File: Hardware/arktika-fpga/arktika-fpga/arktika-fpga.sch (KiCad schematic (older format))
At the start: 4 parts

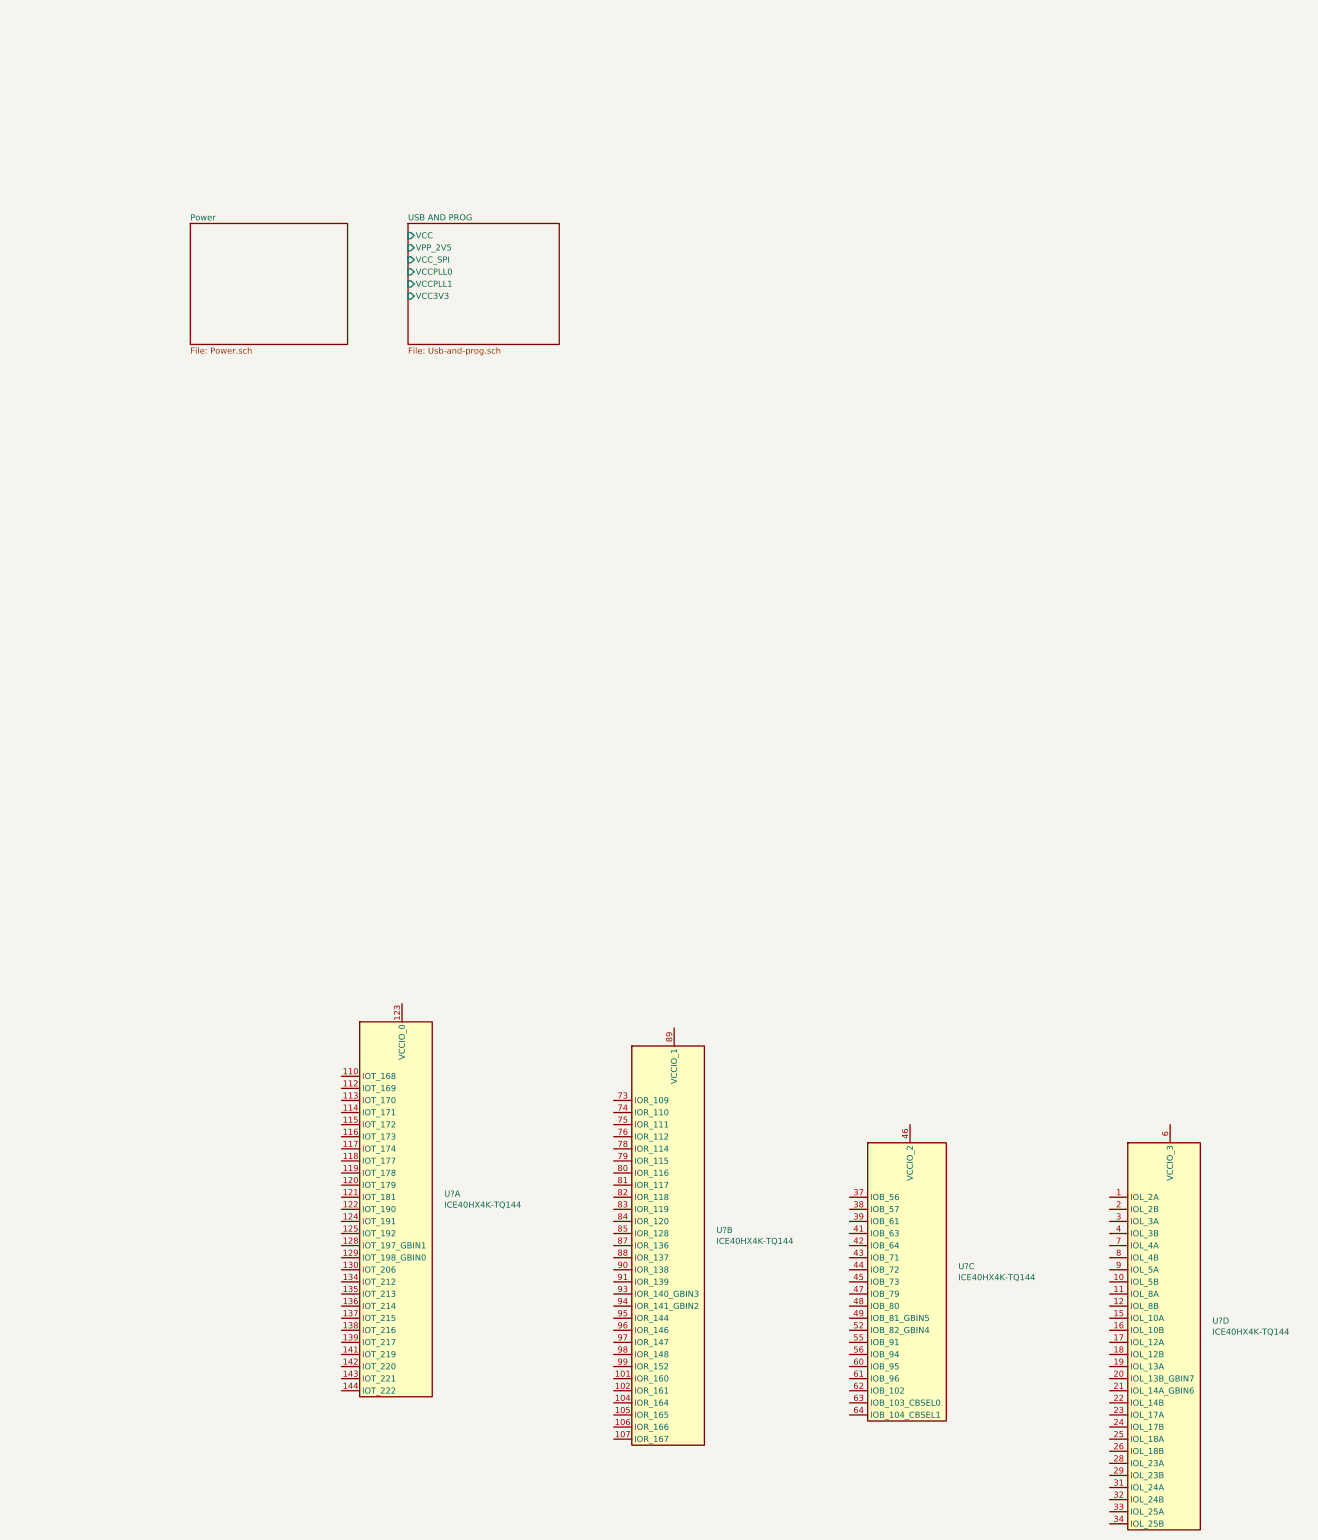
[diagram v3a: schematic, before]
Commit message: Added designators, some io, and some peripherals
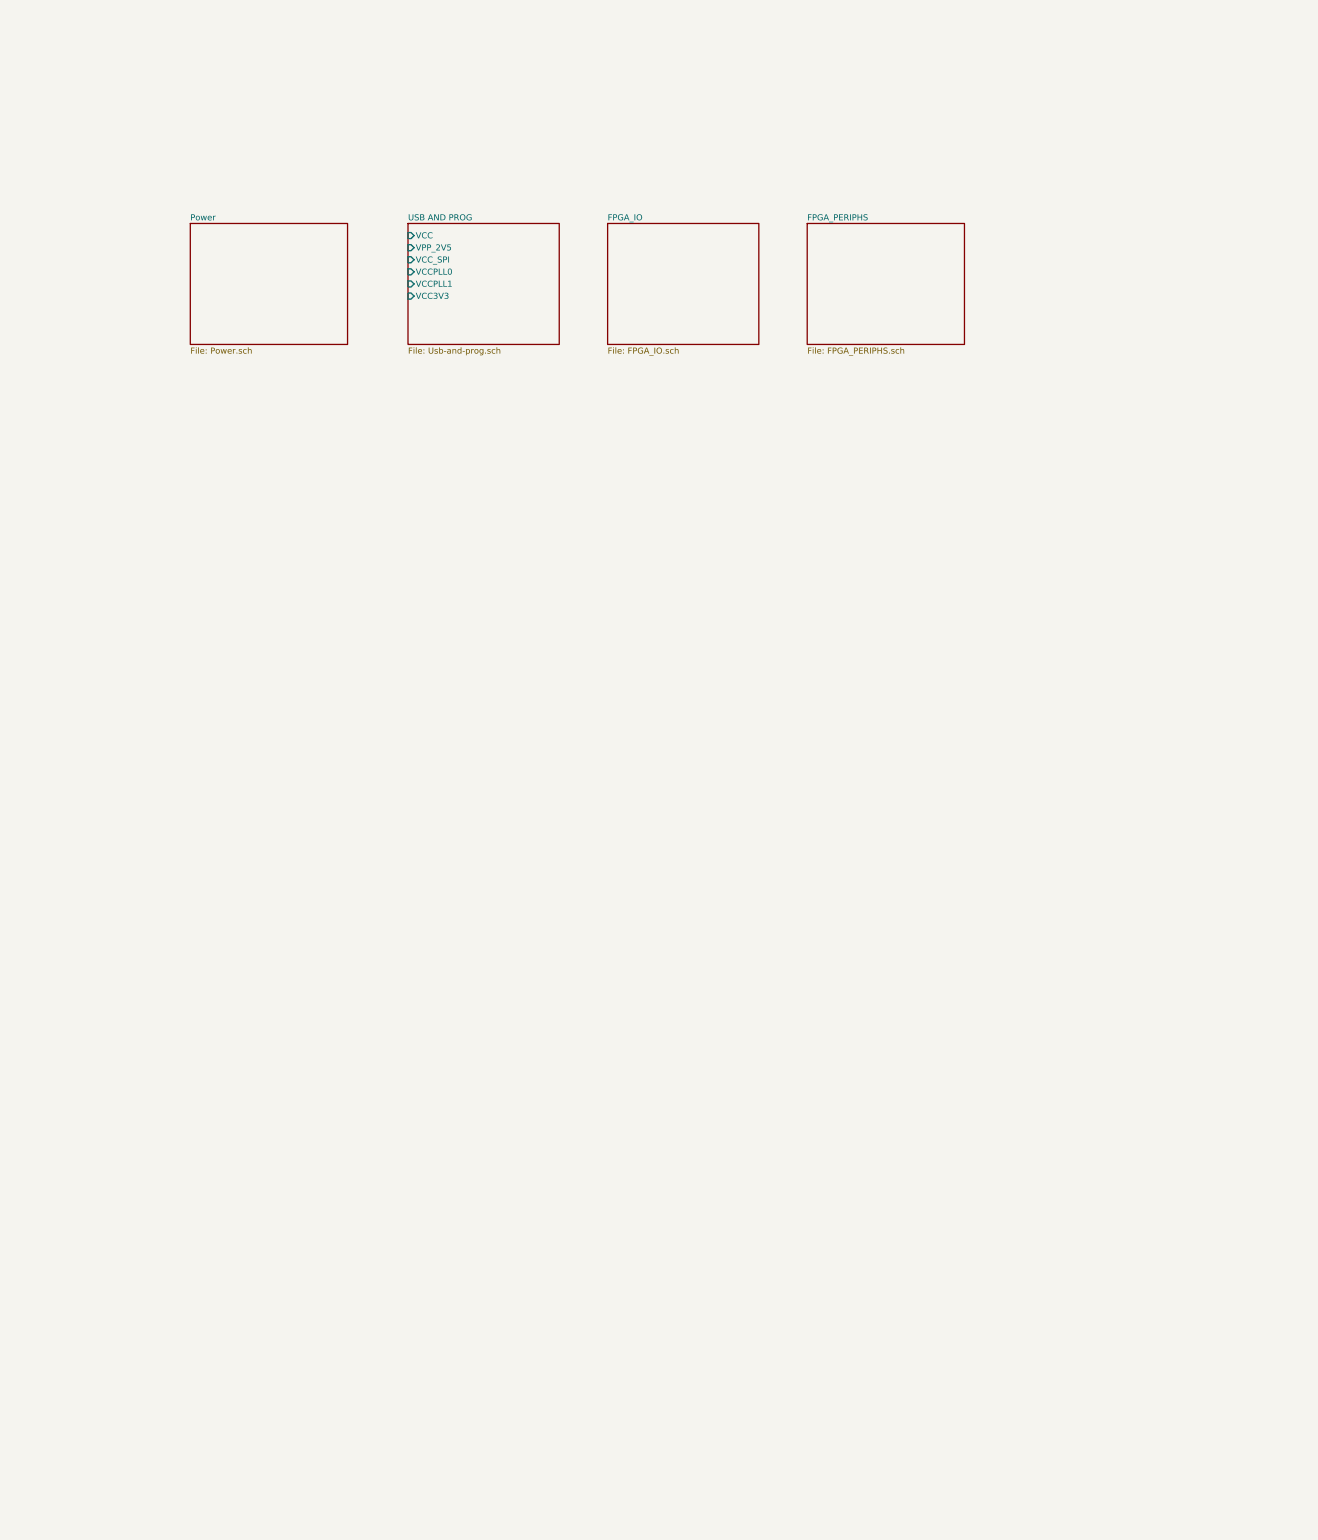
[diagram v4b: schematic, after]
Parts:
- removed U? (x4): ICE40HX4K-TQ144, Package_QFP:TQFP-144_20x20mm_P0.5mm, symbol FPGA_Lattice:ICE40HX4K-TQ144
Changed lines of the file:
@@
 $Descr A4 11693 8268
 encoding utf-8
-Sheet 1 3
+Sheet 1 5
 Title "Arktika FPGA"
-Date "2020-07-26"
+Date "2020-07-28"
 Rev ""
 Comp "Author: Afonso Muralha"
@@
 Comment4 ""
 $EndDescr
-$Comp
-L FPGA_Lattice:ICE40HX4K-TQ144 U?
-U 1 1 5F1D1844
-P 4300 11350
-F 0 "U?" H 4649 11578 50  0000 L CNN
-F 1 "ICE40HX4K-TQ144" H 4649 11487 50  0000 L CNN
-F 2 "Package_QFP:TQFP-144_20x20mm_P0.5mm" H 5300 9450 50  0001 R CNN
-F 3 "http://www.latticesemi.com/Products/FPGAandCPLD/iCE40" H 3300 13850 50  0001 C CNN
-	1    4300 11350
-	1    0    0    -1
-$EndComp
-$Comp
-L FPGA_Lattice:ICE40HX4K-TQ144 U?
-U 2 1 5F1D412B
-P 6550 11650
-F 0 "U?" H 6899 11878 50  0000 L CNN
-F 1 "ICE40HX4K-TQ144" H 6899 11787 50  0000 L CNN
-F 2 "Package_QFP:TQFP-144_20x20mm_P0.5mm" H 7550 9750 50  0001 R CNN
-F 3 "http://www.latticesemi.com/Products/FPGAandCPLD/iCE40" H 5550 14150 50  0001 C CNN
-	2    6550 11650
-	1    0    0    -1
-$EndComp
-$Comp
-L FPGA_Lattice:ICE40HX4K-TQ144 U?
-U 3 1 5F1D7E9E
-P 8500 11950
-F 0 "U?" H 8899 12178 50  0000 L CNN
-F 1 "ICE40HX4K-TQ144" H 8899 12087 50  0000 L CNN
-F 2 "Package_QFP:TQFP-144_20x20mm_P0.5mm" H 9500 10050 50  0001 R CNN
-F 3 "http://www.latticesemi.com/Products/FPGAandCPLD/iCE40" H 7500 14450 50  0001 C CNN
-	3    8500 11950
-	1    0    0    -1
-$EndComp
-$Comp
-L FPGA_Lattice:ICE40HX4K-TQ144 U?
-U 4 1 5F1DC6C8
-P 10650 12350
-F 0 "U?" H 10999 12528 50  0000 L CNN
-F 1 "ICE40HX4K-TQ144" H 10999 12437 50  0000 L CNN
-F 2 "Package_QFP:TQFP-144_20x20mm_P0.5mm" H 11650 10450 50  0001 R CNN
-F 3 "http://www.latticesemi.com/Products/FPGAandCPLD/iCE40" H 9650 14850 50  0001 C CNN
-	4    10650 12350
-	1    0    0    -1
-$EndComp
 $Sheet
 S 2550 3100 1300 1000
@@
 F7 "VCC3V3" I L 4350 3700 50
 $EndSheet
+$Sheet
+S 6000 3100 1250 1000
+U 5F516611
+F0 "FPGA_IO" 50
+F1 "FPGA_IO.sch" 50
+$EndSheet
+$Sheet
+S 7650 3100 1300 1000
+U 5F72015E
+F0 "FPGA_PERIPHS" 50
+F1 "FPGA_PERIPHS.sch" 50
+$EndSheet
 $EndSCHEMATC

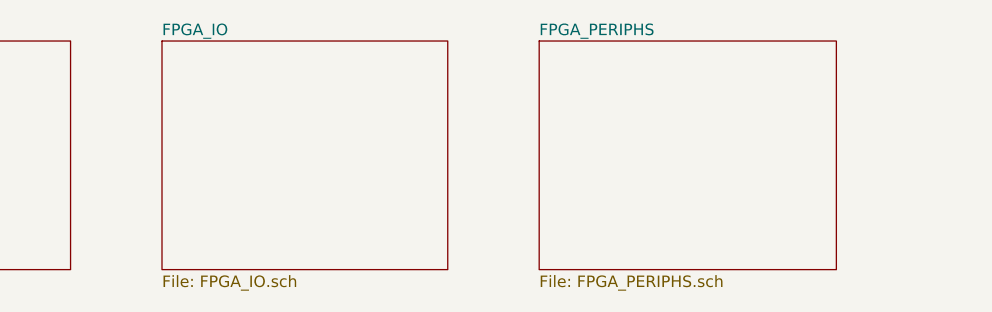
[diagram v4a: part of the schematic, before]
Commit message: Minor fixes, added peripheral buses, added annotations and added crystal datasheets
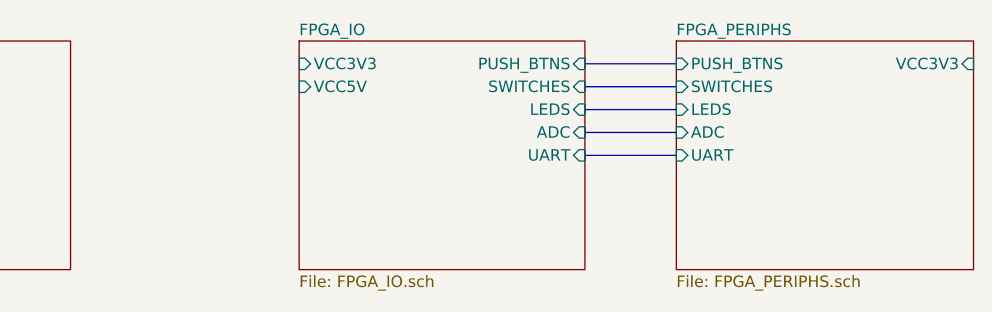
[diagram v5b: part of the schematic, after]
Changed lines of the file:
@@
 Sheet 1 5
 Title "Arktika FPGA"
-Date "2020-07-28"
+Date "2020-07-29"
 Rev ""
 Comp "Author: Afonso Muralha"
@@
 $EndSheet
 $Sheet
-S 6000 3100 1250 1000
+S 6600 3100 1250 1000
 U 5F516611
 F0 "FPGA_IO" 50
 F1 "FPGA_IO.sch" 50
+F2 "VCC3V3" I L 6600 3200 50
+F3 "VCC5V" I L 6600 3300 50
+F4 "PUSH_BTNS" I R 7850 3200 50
+F5 "SWITCHES" I R 7850 3300 50
+F6 "LEDS" I R 7850 3400 50
+F7 "ADC" I R 7850 3500 50
+F8 "UART" I R 7850 3600 50
 $EndSheet
 $Sheet
-S 7650 3100 1300 1000
+S 8250 3100 1300 1000
 U 5F72015E
 F0 "FPGA_PERIPHS" 50
 F1 "FPGA_PERIPHS.sch" 50
+F2 "PUSH_BTNS" I L 8250 3200 50
+F3 "SWITCHES" I L 8250 3300 50
+F4 "LEDS" I L 8250 3400 50
+F5 "ADC" I L 8250 3500 50
+F6 "UART" I L 8250 3600 50
+F7 "VCC3V3" I R 9550 3200 50
 $EndSheet
+Wire Bus Line
+	7850 3200 8250 3200
+Wire Bus Line
+	7850 3300 8250 3300
+Wire Bus Line
+	7850 3400 8250 3400
+Wire Bus Line
+	7850 3500 8250 3500
+Wire Bus Line
+	7850 3600 8250 3600
 $EndSCHEMATC

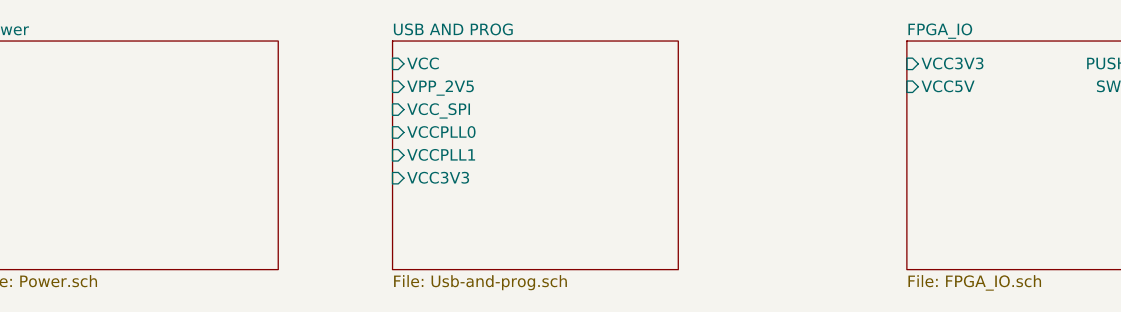
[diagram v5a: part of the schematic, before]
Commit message: Added alternate power intput. Update some designators. Added fpga crystal
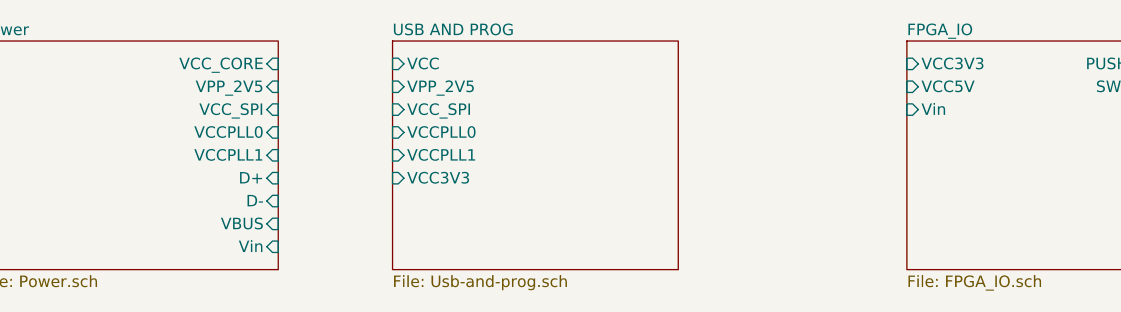
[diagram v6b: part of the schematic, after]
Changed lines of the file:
@@
 F0 "Power" 50
 F1 "Power.sch" 50
+F2 "VCC_CORE" I R 3850 3200 50
+F3 "VPP_2V5" I R 3850 3300 50
+F4 "VCC_SPI" I R 3850 3400 50
+F5 "VCCPLL0" I R 3850 3500 50
+F6 "VCCPLL1" I R 3850 3600 50
+F7 "D+" I R 3850 3700 50
+F8 "D-" I R 3850 3800 50
+F9 "VBUS" I R 3850 3900 50
+F10 "Vin" I R 3850 4000 50
 $EndSheet
 $Sheet
@@
 F7 "ADC" I R 7850 3500 50
 F8 "UART" I R 7850 3600 50
+F9 "Vin" I L 6600 3400 50
 $EndSheet
 $Sheet

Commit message: Misc changes and fixes
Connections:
- net labels added: GND, VCC3V3, VCC5V, VIN
- wire segments 0 -> 19
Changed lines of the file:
@@
 $EndDescr
 $Sheet
-S 2550 3100 1300 1000
+S 2550 3100 1300 1050
 U 5F3E98C5
 F0 "Power" 50
@@
 F7 "D+" I R 3850 3700 50
 F8 "D-" I R 3850 3800 50
-F9 "VBUS" I R 3850 3900 50
-F10 "Vin" I R 3850 4000 50
+F9 "Vin" I R 3850 4100 50
+F10 "VCC3V3" I R 3850 4000 50
+F11 "VCC5V" I R 3850 3900 50
+F12 "GND" I L 2550 4050 50
 $EndSheet
 $Sheet
@@
 F0 "USB AND PROG" 50
 F1 "Usb-and-prog.sch" 50
-F2 "VCC" I L 4350 3200 50
-F3 "VPP_2V5" I L 4350 3300 50
-F4 "VCC_SPI" I L 4350 3400 50
-F5 "VCCPLL0" I L 4350 3500 50
-F6 "VCCPLL1" I L 4350 3600 50
-F7 "VCC3V3" I L 4350 3700 50
+F2 "VPP_2V5" I L 4350 3300 50
+F3 "VCC_SPI" I L 4350 3400 50
+F4 "VCCPLL0" I L 4350 3500 50
+F5 "VCCPLL1" I L 4350 3600 50
+F6 "VCC3V3" I L 4350 4000 50
+F7 "VCC_CORE" I L 4350 3200 50
+F8 "D+" I L 4350 3700 50
+F9 "D-" I L 4350 3800 50
+F10 "VBUS" I L 4350 3900 50
+F11 "GND" I R 5600 4050 50
 $EndSheet
 $Sheet
-S 6600 3100 1250 1000
+S 6300 3100 1250 1000
 U 5F516611
 F0 "FPGA_IO" 50
 F1 "FPGA_IO.sch" 50
-F2 "VCC3V3" I L 6600 3200 50
-F3 "VCC5V" I L 6600 3300 50
-F4 "PUSH_BTNS" I R 7850 3200 50
-F5 "SWITCHES" I R 7850 3300 50
-F6 "LEDS" I R 7850 3400 50
-F7 "ADC" I R 7850 3500 50
-F8 "UART" I R 7850 3600 50
-F9 "Vin" I L 6600 3400 50
+F2 "VCC3V3" I L 6300 3200 50
+F3 "VCC5V" I L 6300 3300 50
+F4 "PUSH_BTNS" I R 7550 3200 50
+F5 "SWITCHES" I R 7550 3300 50
+F6 "LEDS" I R 7550 3400 50
+F7 "ADC" I R 7550 3500 50
+F8 "UART" I R 7550 3600 50
+F9 "Vin" I L 6300 3400 50
+F10 "Buzzer" I R 7550 3700 50
+F11 "GND" I L 6300 4050 50
 $EndSheet
 $Sheet
-S 8250 3100 1300 1000
+S 7950 3100 1300 1000
 U 5F72015E
 F0 "FPGA_PERIPHS" 50
 F1 "FPGA_PERIPHS.sch" 50
-F2 "PUSH_BTNS" I L 8250 3200 50
-F3 "SWITCHES" I L 8250 3300 50
-F4 "LEDS" I L 8250 3400 50
-F5 "ADC" I L 8250 3500 50
-F6 "UART" I L 8250 3600 50
-F7 "VCC3V3" I R 9550 3200 50
+F2 "PUSH_BTNS" I L 7950 3200 50
+F3 "SWITCHES" I L 7950 3300 50
+F4 "LEDS" I L 7950 3400 50
+F5 "ADC" I L 7950 3500 50
+F6 "UART" I L 7950 3600 50
+F7 "VCC3V3" I R 9250 3200 50
+F8 "Buzzer" I L 7950 3700 50
+F9 "GND" I R 9250 4050 50
 $EndSheet
 Wire Bus Line
-	7850 3200 8250 3200
+	7550 3200 7950 3200
 Wire Bus Line
-	7850 3300 8250 3300
+	7550 3300 7950 3300
 Wire Bus Line
-	7850 3400 8250 3400
+	7550 3400 7950 3400
 Wire Bus Line
-	7850 3500 8250 3500
+	7550 3500 7950 3500
 Wire Bus Line
-	7850 3600 8250 3600
+	7550 3600 7950 3600
+Wire Wire Line
+	3850 3200 4350 3200
+Wire Wire Line
+	4350 3300 3850 3300
+Wire Wire Line
+	3850 3400 4350 3400
+Wire Wire Line
+	4350 3500 3850 3500
+Wire Wire Line
+	3850 3600 4350 3600
+Wire Wire Line
+	4350 3700 3850 3700
+Wire Wire Line
+	3850 3800 4350 3800
+Wire Wire Line
+	3850 3900 4350 3900
+Wire Wire Line
+	3850 4000 4350 4000
+Text Label 3950 4000 0    50   ~ 0
+VCC3V3
+Text Label 3950 3900 0    50   ~ 0
+VCC5V
+Wire Wire Line
+	3850 4100 4300 4100
+Text Label 3950 4100 0    50   ~ 0
+VIN
+Text Label 5900 3400 0    50   ~ 0
+VIN
+Text Label 5900 3200 0    50   ~ 0
+VCC3V3
+Text Label 5900 3300 0    50   ~ 0
+VCC5V
+Wire Wire Line
+	5900 3200 6300 3200
+Wire Wire Line
+	6300 3300 5900 3300
+Wire Wire Line
+	5900 3400 6300 3400
+Text Label 9400 3200 0    50   ~ 0
+VCC3V3
+Wire Wire Line
+	9400 3200 9250 3200
+Wire Wire Line
+	7550 3700 7950 3700
+Wire Wire Line
+	2250 4050 2550 4050
+$Comp
+L power:GND #PWR0101
+U 1 1 5F2E4558
+P 2250 4050
+AR Path="/5F2E4558" Ref="#PWR0101"  Part="1"
+AR Path="/5F3E98C5/5F2E4558" Ref="#PWR?"  Part="1"
+F 0 "#PWR0101" H 2250 3800 50  0001 C CNN
+F 1 "GND" H 2250 3900 50  0000 C CNN
+F 2 "" H 2250 4050 50  0001 C CNN
+F 3 "" H 2250 4050 50  0001 C CNN
+	1    2250 4050
+	-1   0    0    -1
+$EndComp
+Wire Wire Line
+	5600 4050 5950 4050
+$Comp
+L power:GND #PWR0102
+U 1 1 5F2E4A9A
+P 5950 4050
+AR Path="/5F2E4A9A" Ref="#PWR0102"  Part="1"
+AR Path="/5F3E98C5/5F2E4A9A" Ref="#PWR?"  Part="1"
+F 0 "#PWR0102" H 5950 3800 50  0001 C CNN
+F 1 "GND" H 5950 3900 50  0000 C CNN
+F 2 "" H 5950 4050 50  0001 C CNN
+F 3 "" H 5950 4050 50  0001 C CNN
+	1    5950 4050
+	-1   0    0    -1
+$EndComp
+Connection ~ 5950 4050
+Wire Wire Line
+	5950 4050 6300 4050
+Wire Wire Line
+	9550 4050 9250 4050
+$Comp
+L power:GND #PWR0103
+U 1 1 5F2E5C47
+P 9550 4050
+AR Path="/5F2E5C47" Ref="#PWR0103"  Part="1"
+AR Path="/5F3E98C5/5F2E5C47" Ref="#PWR?"  Part="1"
+F 0 "#PWR0103" H 9550 3800 50  0001 C CNN
+F 1 "GND" H 9550 3900 50  0000 C CNN
+F 2 "" H 9550 4050 50  0001 C CNN
+F 3 "" H 9550 4050 50  0001 C CNN
+	1    9550 4050
+	1    0    0    -1
+$EndComp
 $EndSCHEMATC
